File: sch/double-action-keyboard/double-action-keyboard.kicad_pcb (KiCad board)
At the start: 2 copper layers, 125 x 68 mm, 125 parts, among them U1 Pico

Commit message: ダイオードの配置と配線を行いました。
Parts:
- removed H1, H2, H3, H4: MountingHole_Pad, MountingHole:MountingHole_3.2mm_M3_Pad
- added C1: 1u, Capacitor_SMD:C_0603_1608Metric_Pad1.08x0.95mm_HandSolder, B.Cu at (96.5, 58.0)
- added C2: 1u, Capacitor_SMD:C_0603_1608Metric_Pad1.08x0.95mm_HandSolder, B.Cu at (98.1, 60.5)
- added C3: 1u, Capacitor_SMD:C_0603_1608Metric_Pad1.08x0.95mm_HandSolder, B.Cu at (101.0, 58.5)
- added C4: 1u, Capacitor_SMD:C_0603_1608Metric_Pad1.08x0.95mm_HandSolder, B.Cu at (82.1, 71.0)
- added C5: 1u, Capacitor_SMD:C_0603_1608Metric_Pad1.08x0.95mm_HandSolder, B.Cu at (74.6, 67.5)
- added C6: 1u, Capacitor_SMD:C_0603_1608Metric_Pad1.08x0.95mm_HandSolder, B.Cu at (77.1, 70.5)
- added D81: D, Diode_SMD:D_SOD-123, F.Cu at (143.8, 72.5)
- added J1: Conn_01x02, Connector_JST:JST_XH_B2B-XH-A_1x02_P2.50mm_Vertical, F.Cu at (137.8, 72.5)
- added R1: 10k, Resistor_SMD:R_0603_1608Metric_Pad0.98x0.95mm_HandSolder, B.Cu at (86.5, 69.6)
- added R2: 10k, Resistor_SMD:R_0603_1608Metric_Pad0.98x0.95mm_HandSolder, B.Cu at (89.0, 69.6)
- added R3: 10k, Resistor_SMD:R_0603_1608Metric_Pad0.98x0.95mm_HandSolder, B.Cu at (91.5, 69.6)
- added R7: 1k, Resistor_SMD:R_0603_1608Metric_Pad0.98x0.95mm_HandSolder, B.Cu at (66.0, 67.0)
- added R8: 0, Resistor_SMD:R_0603_1608Metric_Pad0.98x0.95mm_HandSolder, B.Cu at (97.9, 66.5)
- added REF1: MountingHole_3.2mm_M3, MountingHole:MountingHole_3.2mm_M3, F.Cu at (53.5, 53.5)
- added REF1: MountingHole_3.2mm_M3, MountingHole:MountingHole_3.2mm_M3, F.Cu at (140.0, 53.5)
- added REF1: MountingHole_3.2mm_M3, MountingHole:MountingHole_3.2mm_M3, F.Cu at (196.5, 118.5)
- added REF2: MountingHole_3.2mm_M3, MountingHole:MountingHole_3.2mm_M3, F.Cu at (53.5, 118.5)
- added U2: AQM1602XA-RN-GBW, AQM1602:AQM1602XA-RN-GBW, F.Cu at (97.4, 55.0)
- added U3: AQM1602Y-NLW-FBW, AQM1602:AQM1602Y-NLW-FBW, F.Cu at (81.2, 75.0)
- D1, D10, D11, D12, D13, D14, D15, D16, D17, D18, D19, D2, D20, D21, D22, D23, D24, D25, D26, D27, D28, D29, D3, D30, D31, D32, D33, D34, D35, D36, D37, D38, D39, D4, D40, D41, D42, D43, D44, D45, D46, D47, D48, D49, D5, D50, D51, D52, D53, D54, D55, D56, D57, D58, D59, D6, D60, D61, D62, D63, D64, D65, D66, D67, D68, D69, D7, D70, D71, D72, D73, D74, D75, D76, D77, D78, D79, D8, D80, D9: moved to B.Cu
- U1: footprint MCU_RaspberryPi_and_Boards:RPi_Pico_SMD_TH -> my_pico_smd:pico_no_dbg_smd_th
- moved D79 87.4 mm to (175.5, 115.5), turned to -90 degrees
- moved D80 87.1 mm to (180.5, 115.5), turned to -90 degrees
- moved D77 86.3 mm to (162.5, 115.5), turned to -90 degrees
- moved D78 86.1 mm to (167.5, 115.5), turned to -90 degrees
- moved D75 85.4 mm to (149.5, 115.5), turned to -90 degrees
- moved D76 85.1 mm to (154.5, 115.5), turned to -90 degrees
- moved D73 84.6 mm to (136.5, 115.5), turned to -90 degrees
- moved D74 84.3 mm to (141.5, 115.5), turned to -90 degrees
- moved D71 83.5 mm to (123.5, 115.5), turned to -90 degrees
- moved D72 83.3 mm to (128.5, 115.5), turned to -90 degrees
- moved D69 82.9 mm to (110.5, 115.5), turned to -90 degrees
- moved D70 82.4 mm to (115.5, 115.5), turned to -90 degrees
- moved D67 82.2 mm to (97.5, 115.5), turned to -90 degrees
- moved D68 81.9 mm to (102.5, 115.5), turned to -90 degrees
- moved D65 81.4 mm to (84.5, 115.5), turned to -90 degrees
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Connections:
- D11 pad 2: /COL0 -> /COL10
- D12 pad 2: /COL1 -> /COL11
- D13 pad 2: /COL2 -> /COL12
- D14 pad 2: /COL3 -> /COL13
- D15 pad 2: /COL4 -> /COL14
- D16 pad 2: /COL5 -> /COL15
- D17 pad 2: /COL6 -> /COL16
- D18 pad 2: /COL7 -> /COL17
- D19 pad 2: /COL8 -> /COL18
- D20 pad 2: /COL9 -> /COL19
- D31 pad 2: /COL0 -> /COL10
- D32 pad 2: /COL1 -> /COL11
- D33 pad 2: /COL2 -> /COL12
- D34 pad 2: /COL3 -> /COL13
- D35 pad 2: /COL4 -> /COL14
- D36 pad 2: /COL5 -> /COL15
- D37 pad 2: /COL6 -> /COL16
- D38 pad 2: /COL7 -> /COL17
- D39 pad 2: /COL8 -> /COL18
- D40 pad 2: /COL9 -> /COL19
- D51 pad 2: /COL0 -> /COL10
- D52 pad 2: /COL1 -> /COL11
- D53 pad 2: /COL2 -> /COL12
- D54 pad 2: /COL3 -> /COL13
- D55 pad 2: /COL4 -> /COL14
- D56 pad 2: /COL5 -> /COL15
- D57 pad 2: /COL6 -> /COL16
- D58 pad 2: /COL7 -> /COL17
- D59 pad 2: /COL8 -> /COL18
- D60 pad 2: /COL9 -> /COL19
- D71 pad 2: /COL0 -> /COL10
- D72 pad 2: /COL1 -> /COL11
- D73 pad 2: /COL2 -> /COL12
- D74 pad 2: /COL3 -> /COL13
- D75 pad 2: /COL4 -> /COL14
- D76 pad 2: /COL5 -> /COL15
- D77 pad 2: /COL6 -> /COL16
- D78 pad 2: /COL7 -> /COL17
- D79 pad 2: /COL8 -> /COL18
- D80 pad 2: /COL9 -> /COL19
- SW10 pad 3: /ROW1 -> /ROW0
- SW11 pad 3: /ROW2 -> /ROW1
- SW12 pad 3: /ROW2 -> /ROW1
- SW13 pad 3: /ROW2 -> /ROW1
- SW14 pad 3: /ROW2 -> /ROW1
- SW15 pad 3: /ROW2 -> /ROW1
- SW16 pad 3: /ROW3 -> /ROW1
- SW17 pad 3: /ROW3 -> /ROW1
- SW18 pad 3: /ROW3 -> /ROW1
- SW19 pad 3: /ROW3 -> /ROW1
- SW20 pad 3: /ROW3 -> /ROW1
- SW21 pad 3: /ROW4 -> /ROW2
- SW22 pad 3: /ROW4 -> /ROW2
- SW23 pad 3: /ROW4 -> /ROW2
- SW24 pad 3: /ROW4 -> /ROW2
- SW25 pad 3: /ROW4 -> /ROW2
- SW26 pad 3: /ROW5 -> /ROW2
- SW27 pad 3: /ROW5 -> /ROW2
- SW28 pad 3: /ROW5 -> /ROW2
- SW29 pad 3: /ROW5 -> /ROW2
- SW30 pad 3: /ROW5 -> /ROW2
- SW31 pad 3: /ROW6 -> /ROW3
- SW32 pad 3: /ROW6 -> /ROW3
- SW33 pad 3: /ROW6 -> /ROW3
- SW34 pad 3: /ROW6 -> /ROW3
- SW35 pad 3: /ROW6 -> /ROW3
- SW36 pad 3: /ROW7 -> /ROW3
- SW37 pad 3: /ROW7 -> /ROW3
- SW38 pad 3: /ROW7 -> /ROW3
- SW39 pad 3: /ROW7 -> /ROW3
- SW40 pad 3: /ROW7 -> /ROW3
- SW6 pad 3: /ROW1 -> /ROW0
- SW7 pad 3: /ROW1 -> /ROW0
- SW8 pad 3: /ROW1 -> /ROW0
- SW9 pad 3: /ROW1 -> /ROW0
- U1 pad 1: /COL0 -> /ROW3
- U1 pad 10: /COL7 -> /COL6
- U1 pad 11: /COL8 -> /COL5
- U1 pad 12: /COL9 -> /COL4
- U1 pad 14: /ROW0 -> /COL3
- U1 pad 15: /ROW1 -> /COL2
- U1 pad 16: /ROW2 -> /COL1
- U1 pad 17: /ROW3 -> /COL0
- U1 pad 19: /ROW4 -> /LCD_I2C_SDA
- U1 pad 2: /COL1 -> /ROW2
- U1 pad 20: /ROW5 -> /LCD_I2C_SCL
- U1 pad 21: /ROW7 -> /COL10
- U1 pad 22: /ROW6 -> /COL11
- U1 pad 24: unconnected-(U1-GPIO18-Pad24) -> /COL12
- U1 pad 25: unconnected-(U1-GPIO19-Pad25) -> /COL13
- U1 pad 26: unconnected-(U1-GPIO20-Pad26) -> /COL14
- U1 pad 27: unconnected-(U1-GPIO21-Pad27) -> /COL15
- U1 pad 29: unconnected-(U1-GPIO22-Pad29) -> /COL16
- U1 pad 31: unconnected-(U1-GPIO26_ADC0-Pad31) -> /COL17
- U1 pad 32: unconnected-(U1-GPIO27_ADC1-Pad32) -> /COL18
- U1 pad 34: unconnected-(U1-GPIO28_ADC2-Pad34) -> /COL19
- U1 pad 36: unconnected-(U1-3V3-Pad36) -> +3.3V
- U1 pad 39: unconnected-(U1-VSYS-Pad39) -> Net-(D81-K)
- U1 pad 4: /COL2 -> /ROW1
- U1 pad 5: /COL3 -> /ROW0
- U1 pad 6: /COL4 -> /COL9
- U1 pad 7: /COL5 -> /COL8
- U1 pad 9: /COL6 -> /COL7
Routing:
- net /ROW3: track 0.00 -> 220.6 mm
- net /ROW2: track 0.00 -> 208.0 mm
- net /ROW1: track 0.00 -> 193.2 mm
- net /ROW0: track 0.00 -> 180.1 mm
- net /COL0: track 0.00 -> 166.6 mm
- net +3.3V: track 0.00 -> 163.9 mm, vias 0 -> 2
- net /COL1: track 0.00 -> 162.1 mm
- net /COL2: track 0.00 -> 156.4 mm
- net /COL3: track 0.00 -> 154.2 mm
- net /COL4: track 0.00 -> 151.2 mm
- net /COL5: track 0.00 -> 148.8 mm
- net /COL6: track 0.00 -> 143.0 mm
- net /COL7: track 0.00 -> 140.9 mm
- net /COL8: track 0.00 -> 137.6 mm
- net /COL9: track 0.00 -> 136.1 mm
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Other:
- board size 125 x 68 mm -> 150 x 72 mm

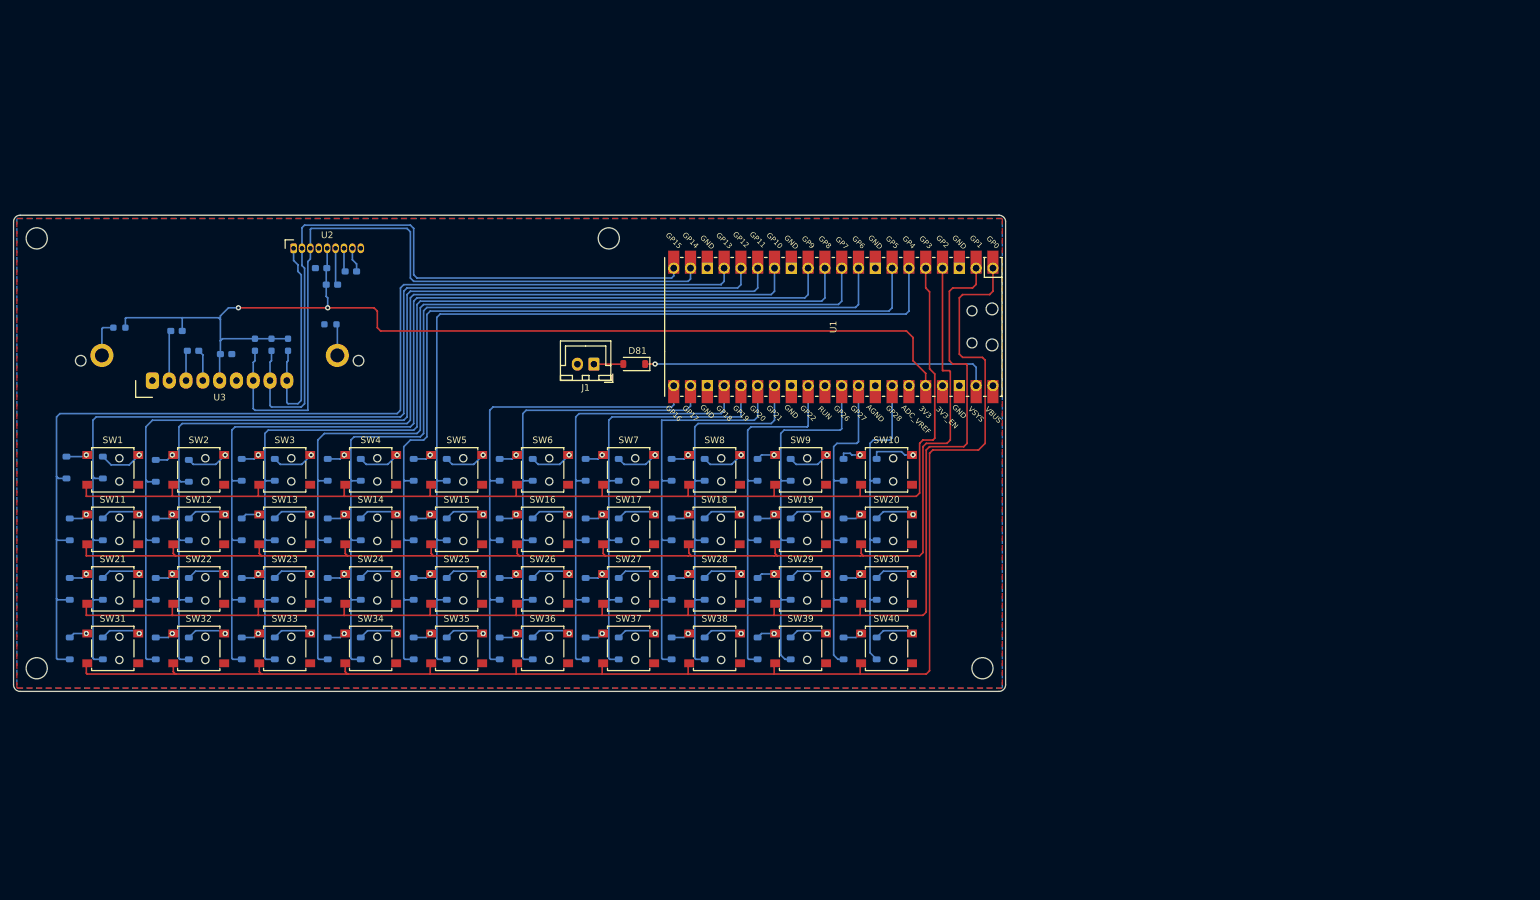
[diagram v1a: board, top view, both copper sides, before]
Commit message: KiCad 8.0にアップデートしました。 部品配置をやり直し中。
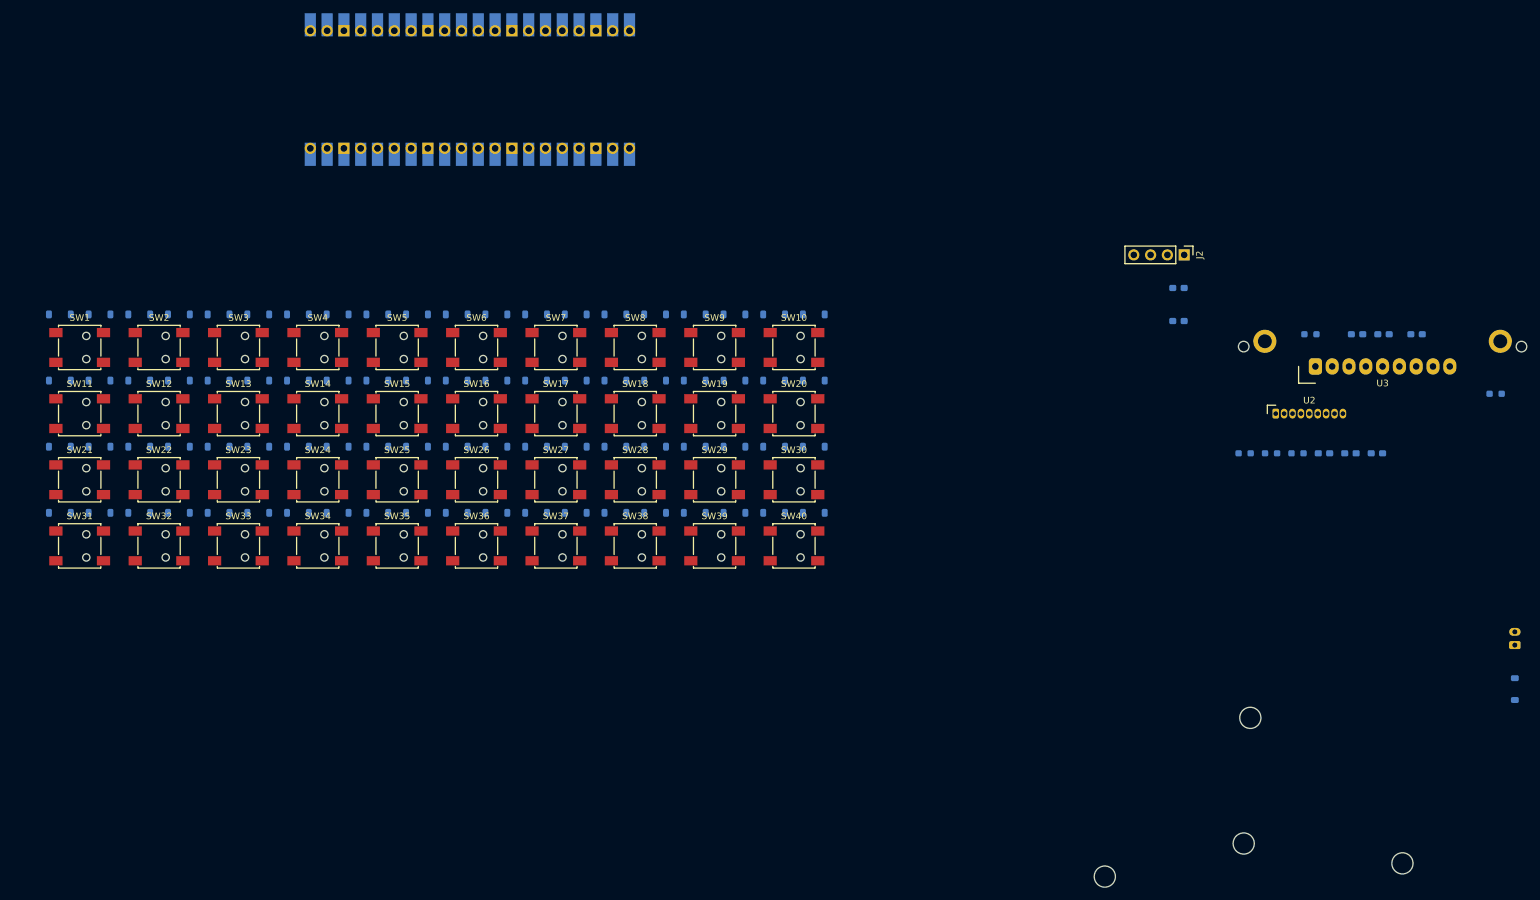
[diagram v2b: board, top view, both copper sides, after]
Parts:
- removed R7: 1k, Resistor_SMD:R_0603_1608Metric_Pad0.98x0.95mm_HandSolder
- removed R8: 0, Resistor_SMD:R_0603_1608Metric_Pad0.98x0.95mm_HandSolder
- added C7: 10u, Capacitor_SMD:C_0603_1608Metric_Pad1.08x0.95mm_HandSolder, B.Cu at (226.1, 61.0)
- added C8: 0.1u, Capacitor_SMD:C_0603_1608Metric_Pad1.08x0.95mm_HandSolder, B.Cu at (226.1, 66.0)
- added J2: Conn_01x04, Connector_PinHeader_2.54mm:PinHeader_1x04_P2.54mm_Vertical, F.Cu at (227.0, 56.0)
- added R4: 1k, Resistor_SMD:R_0603_1608Metric_Pad0.98x0.95mm_HandSolder, B.Cu at (246.1, 68.0)
- added R5: 0, Resistor_SMD:R_0603_1608Metric_Pad0.98x0.95mm_HandSolder, B.Cu at (274.1, 77.0)
- D1: value 1N4148W -> D
- D81: value D -> 1N4148W; moved to B.Cu
- J1: footprint Connector_JST:JST_XH_B2B-XH-A_1x02_P2.50mm_Vertical -> Connector_JST:JST_PH_B2B-PH-K_1x02_P2.00mm_Vertical; moved to B.Cu
- U1: moved to B.Cu
- moved D1 221.5 mm to (277.0, 121.7), turned to 90 degrees
- moved REF1 188.1 mm to (215.0, 150.0)
- moved REF2 184.4 mm to (236.0, 145.0)
- moved C4 180.0 mm to (262.1, 68.0)
- moved C6 180.0 mm to (257.1, 68.0)
- moved C5 178.5 mm to (253.1, 68.0)
- moved U3 175.9 mm to (257.0, 72.9)
- moved R1 158.5 mm to (244.1, 86.0), turned to 0 degrees
- moved C3 157.6 mm to (256.1, 86.0)
- moved C2 156.1 mm to (252.1, 86.0)
- moved C1 154.2 mm to (248.1, 86.0)
- moved REF1 152.7 mm to (260.0, 148.0)
- moved R2 152.0 mm to (240.1, 86.0), turned to 0 degrees
- moved U2 150.6 mm to (245.9, 80.0)
- moved J1 145.6 mm to (277.0, 115.0), turned to 90 degrees
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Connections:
- D1 pad 2: /COL0 -> Net-(D1-A)
- D10 pad 2: /COL9 -> /COL8
- D11 pad 2: /COL10 -> /COL9
- D12 pad 2: /COL11 -> /COL10
- D13 pad 2: /COL12 -> /COL11
- D14 pad 2: /COL13 -> /COL12
- D15 pad 2: /COL14 -> /COL13
- D16 pad 2: /COL15 -> /COL14
- D17 pad 2: /COL16 -> /COL15
- D18 pad 2: /COL17 -> /COL16
- D19 pad 2: /COL18 -> /COL17
- D2 pad 2: /COL1 -> /COL0
- D20 pad 2: /COL19 -> /COL18
- D21 pad 2: /COL0 -> /COL19
- D22 pad 2: /COL1 -> /COL0
- D23 pad 2: /COL2 -> /COL1
- D24 pad 2: /COL3 -> /COL2
- D25 pad 2: /COL4 -> /COL3
- D26 pad 2: /COL5 -> /COL4
- D27 pad 2: /COL6 -> /COL5
- D28 pad 2: /COL7 -> /COL6
- D29 pad 2: /COL8 -> /COL7
- D3 pad 2: /COL2 -> /COL1
- D30 pad 2: /COL9 -> /COL8
- D31 pad 2: /COL10 -> /COL9
- D32 pad 2: /COL11 -> /COL10
- D33 pad 2: /COL12 -> /COL11
- D34 pad 2: /COL13 -> /COL12
- D35 pad 2: /COL14 -> /COL13
- D36 pad 2: /COL15 -> /COL14
- D37 pad 2: /COL16 -> /COL15
- D38 pad 2: /COL17 -> /COL16
- D39 pad 2: /COL18 -> /COL17
- D4 pad 2: /COL3 -> /COL2
- D40 pad 2: /COL19 -> /COL18
- D41 pad 2: /COL0 -> /COL19
- D42 pad 2: /COL1 -> /COL0
- D43 pad 2: /COL2 -> /COL1
- D44 pad 2: /COL3 -> /COL2
- D45 pad 2: /COL4 -> /COL3
- D46 pad 2: /COL5 -> /COL4
- D47 pad 2: /COL6 -> /COL5
- D48 pad 2: /COL7 -> /COL6
- D49 pad 2: /COL8 -> /COL7
- D5 pad 2: /COL4 -> /COL3
- D50 pad 2: /COL9 -> /COL8
- D51 pad 2: /COL10 -> /COL9
- D52 pad 2: /COL11 -> /COL10
- D53 pad 2: /COL12 -> /COL11
- D54 pad 2: /COL13 -> /COL12
- D55 pad 2: /COL14 -> /COL13
- D56 pad 2: /COL15 -> /COL14
- D57 pad 2: /COL16 -> /COL15
- D58 pad 2: /COL17 -> /COL16
- D59 pad 2: /COL18 -> /COL17
- D6 pad 2: /COL5 -> /COL4
- D60 pad 2: /COL19 -> /COL18
- D61 pad 2: /COL0 -> /COL19
- D62 pad 2: /COL1 -> /COL0
- D63 pad 2: /COL2 -> /COL1
- D64 pad 2: /COL3 -> /COL2
- D65 pad 2: /COL4 -> /COL3
- D66 pad 2: /COL5 -> /COL4
- D67 pad 2: /COL6 -> /COL5
- D68 pad 2: /COL7 -> /COL6
- D69 pad 2: /COL8 -> /COL7
- D7 pad 2: /COL6 -> /COL5
- D70 pad 2: /COL9 -> /COL8
- D71 pad 2: /COL10 -> /COL9
- D72 pad 2: /COL11 -> /COL10
- D73 pad 2: /COL12 -> /COL11
- D74 pad 2: /COL13 -> /COL12
- D75 pad 2: /COL14 -> /COL13
- D76 pad 2: /COL15 -> /COL14
- D77 pad 2: /COL16 -> /COL15
- D78 pad 2: /COL17 -> /COL16
- D79 pad 2: /COL18 -> /COL17
- D8 pad 2: /COL7 -> /COL6
- D80 pad 2: /COL19 -> /COL18
- D81 pad 2: Net-(D81-A) -> /COL19
- D9 pad 2: /COL8 -> /COL7
- J1 pad 1: Net-(D81-A) -> Net-(D1-A)
- SW1 pad 1: Net-(D2-K) -> Net-(D3-K)
- SW1 pad 2: Net-(D1-K) -> Net-(D2-K)
- SW10 pad 1: Net-(D20-K) -> Net-(D21-K)
- SW10 pad 2: Net-(D19-K) -> Net-(D20-K)
- SW11 pad 1: Net-(D22-K) -> Net-(D23-K)
- SW11 pad 2: Net-(D21-K) -> Net-(D22-K)
- SW12 pad 1: Net-(D24-K) -> Net-(D25-K)
- SW12 pad 2: Net-(D23-K) -> Net-(D24-K)
- SW13 pad 1: Net-(D26-K) -> Net-(D27-K)
- SW13 pad 2: Net-(D25-K) -> Net-(D26-K)
- SW14 pad 1: Net-(D28-K) -> Net-(D29-K)
- SW14 pad 2: Net-(D27-K) -> Net-(D28-K)
- SW15 pad 1: Net-(D30-K) -> Net-(D31-K)
- SW15 pad 2: Net-(D29-K) -> Net-(D30-K)
- SW16 pad 1: Net-(D32-K) -> Net-(D33-K)
- SW16 pad 2: Net-(D31-K) -> Net-(D32-K)
- SW17 pad 1: Net-(D34-K) -> Net-(D35-K)
- SW17 pad 2: Net-(D33-K) -> Net-(D34-K)
- SW18 pad 1: Net-(D36-K) -> Net-(D37-K)
- SW18 pad 2: Net-(D35-K) -> Net-(D36-K)
- SW19 pad 1: Net-(D38-K) -> Net-(D39-K)
- SW19 pad 2: Net-(D37-K) -> Net-(D38-K)
- SW2 pad 1: Net-(D4-K) -> Net-(D5-K)
- SW2 pad 2: Net-(D3-K) -> Net-(D4-K)
- SW20 pad 1: Net-(D40-K) -> Net-(D41-K)
- SW20 pad 2: Net-(D39-K) -> Net-(D40-K)
- SW21 pad 1: Net-(D42-K) -> Net-(D43-K)
- SW21 pad 2: Net-(D41-K) -> Net-(D42-K)
- SW22 pad 1: Net-(D44-K) -> Net-(D45-K)
- SW22 pad 2: Net-(D43-K) -> Net-(D44-K)
- SW23 pad 1: Net-(D46-K) -> Net-(D47-K)
- SW23 pad 2: Net-(D45-K) -> Net-(D46-K)
- SW24 pad 1: Net-(D48-K) -> Net-(D49-K)
- SW24 pad 2: Net-(D47-K) -> Net-(D48-K)
- SW25 pad 1: Net-(D50-K) -> Net-(D51-K)
- SW25 pad 2: Net-(D49-K) -> Net-(D50-K)
- SW26 pad 1: Net-(D52-K) -> Net-(D53-K)
- SW26 pad 2: Net-(D51-K) -> Net-(D52-K)
- SW27 pad 1: Net-(D54-K) -> Net-(D55-K)
- SW27 pad 2: Net-(D53-K) -> Net-(D54-K)
- SW28 pad 1: Net-(D56-K) -> Net-(D57-K)
- SW28 pad 2: Net-(D55-K) -> Net-(D56-K)
- SW29 pad 1: Net-(D58-K) -> Net-(D59-K)
- SW29 pad 2: Net-(D57-K) -> Net-(D58-K)
- SW3 pad 1: Net-(D6-K) -> Net-(D7-K)
- SW3 pad 2: Net-(D5-K) -> Net-(D6-K)
- SW30 pad 1: Net-(D60-K) -> Net-(D61-K)
- SW30 pad 2: Net-(D59-K) -> Net-(D60-K)
- SW31 pad 1: Net-(D62-K) -> Net-(D63-K)
- SW31 pad 2: Net-(D61-K) -> Net-(D62-K)
- SW32 pad 1: Net-(D64-K) -> Net-(D65-K)
- SW32 pad 2: Net-(D63-K) -> Net-(D64-K)
- SW33 pad 1: Net-(D66-K) -> Net-(D67-K)
- SW33 pad 2: Net-(D65-K) -> Net-(D66-K)
- SW34 pad 1: Net-(D68-K) -> Net-(D69-K)
- SW34 pad 2: Net-(D67-K) -> Net-(D68-K)
- SW35 pad 1: Net-(D70-K) -> Net-(D71-K)
- SW35 pad 2: Net-(D69-K) -> Net-(D70-K)
- SW36 pad 1: Net-(D72-K) -> Net-(D73-K)
- SW36 pad 2: Net-(D71-K) -> Net-(D72-K)
- SW37 pad 1: Net-(D74-K) -> Net-(D75-K)
- SW37 pad 2: Net-(D73-K) -> Net-(D74-K)
- SW38 pad 1: Net-(D76-K) -> Net-(D77-K)
- SW38 pad 2: Net-(D75-K) -> Net-(D76-K)
- SW39 pad 1: Net-(D78-K) -> Net-(D79-K)
- SW39 pad 2: Net-(D77-K) -> Net-(D78-K)
- SW4 pad 1: Net-(D8-K) -> Net-(D9-K)
- SW4 pad 2: Net-(D7-K) -> Net-(D8-K)
- SW40 pad 1: Net-(D80-K) -> Net-(D81-K)
- SW40 pad 2: Net-(D79-K) -> Net-(D80-K)
- SW5 pad 1: Net-(D10-K) -> Net-(D11-K)
- SW5 pad 2: Net-(D9-K) -> Net-(D10-K)
- SW6 pad 1: Net-(D12-K) -> Net-(D13-K)
- SW6 pad 2: Net-(D11-K) -> Net-(D12-K)
- SW7 pad 1: Net-(D14-K) -> Net-(D15-K)
- SW7 pad 2: Net-(D13-K) -> Net-(D14-K)
- SW8 pad 1: Net-(D16-K) -> Net-(D17-K)
- SW8 pad 2: Net-(D15-K) -> Net-(D16-K)
- SW9 pad 1: Net-(D18-K) -> Net-(D19-K)
- SW9 pad 2: Net-(D17-K) -> Net-(D18-K)
- U1 pad 1: /ROW3 -> /LCD_I2C_SDA
- U1 pad 10: /COL6 -> /COL11
- U1 pad 11: /COL5 -> /COL12
- U1 pad 12: /COL4 -> /COL13
- U1 pad 14: /COL3 -> /COL14
- U1 pad 15: /COL2 -> /COL15
- U1 pad 16: /COL1 -> /COL16
- U1 pad 17: /COL0 -> /COL17
- U1 pad 19: /LCD_I2C_SDA -> /COL18
- U1 pad 2: /ROW2 -> /LCD_I2C_SCL
- U1 pad 20: /LCD_I2C_SCL -> /COL19
- U1 pad 21: /COL10 -> /COL5
- U1 pad 22: /COL11 -> /COL4
- U1 pad 24: /COL12 -> /COL3
- U1 pad 25: /COL13 -> /COL2
- U1 pad 26: /COL14 -> /COL1
- U1 pad 27: /COL15 -> /COL0
- U1 pad 29: /COL16 -> /ROW0
- U1 pad 31: /COL17 -> /ROW1
- U1 pad 32: /COL18 -> /ROW2
- U1 pad 34: /COL19 -> /ROW3
- U1 pad 39: Net-(D81-K) -> Net-(D1-K)
- U1 pad 4: /ROW1 -> /COL6
- U1 pad 5: /ROW0 -> /COL7
- U1 pad 6: /COL9 -> /COL8
- U1 pad 7: /COL8 -> /COL9
- U1 pad 9: /COL7 -> /COL10
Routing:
- net /ROW3: track 220.6 -> 0.00 mm
- net /ROW2: track 208.0 -> 0.00 mm
- net /ROW1: track 193.2 -> 0.00 mm
- net /ROW0: track 180.1 -> 0.00 mm
- net /COL0: track 166.6 -> 0.00 mm
- net +3.3V: track 163.9 -> 0.28 mm, vias 2 -> 0
- net /COL1: track 162.1 -> 0.00 mm
- net /COL2: track 156.4 -> 0.00 mm
- net /COL3: track 154.2 -> 0.00 mm
- net /COL4: track 151.2 -> 0.00 mm
- net /COL5: track 148.8 -> 0.00 mm
- net /COL6: track 143.0 -> 0.00 mm
- net /COL7: track 140.9 -> 0.00 mm
- net /COL8: track 137.6 -> 0.00 mm
- net /COL9: track 136.1 -> 0.00 mm
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- removed copper zone on B.Cu, net GND
- removed copper zone on F.Cu, net GND
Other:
- board outline removed

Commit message: ざっくり配線しました。 線間はもっと詰める予定。
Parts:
- added C10: 0.1u, Capacitor_SMD:C_0603_1608Metric_Pad1.08x0.95mm_HandSolder, B.Cu at (243.0, 60.0)
- added C9: 10u, Capacitor_SMD:C_0603_1608Metric_Pad1.08x0.95mm_HandSolder, B.Cu at (243.0, 64.0)
- added J3: Conn_01x04, Connector_PinHeader_2.54mm:PinHeader_1x04_P2.54mm_Vertical, F.Cu at (250.0, 56.0)
- added R6: 10k, Resistor_SMD:R_0603_1608Metric_Pad0.98x0.95mm_HandSolder, B.Cu at (156.0, 46.0)
- moved R1 151.8 mm to (106.0, 23.0)
- moved C1 148.7 mm to (110.0, 31.0)
- moved C2 148.7 mm to (114.0, 31.0)
- moved C3 148.7 mm to (118.0, 31.0)
- moved R3 148.4 mm to (100.0, 27.0)
- moved R2 147.4 mm to (106.0, 25.0)
- moved U2 141.8 mm to (114.0, 28.0)
- moved R5 116.6 mm to (162.0, 45.0)
- moved C4 114.3 mm to (150.0, 46.0)
- moved C5 113.3 mm to (142.0, 46.0)
- moved C6 113.3 mm to (146.0, 46.0)
- moved R4 111.7 mm to (137.0, 44.0)
- moved U3 109.6 mm to (150.0, 49.0)
- moved U1 40.8 mm to (80.0, 43.1)
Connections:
- U1 pad 29: /ROW0 -> /ROW3
- U1 pad 31: /ROW1 -> /ROW2
- U1 pad 32: /ROW2 -> /ROW1
- U1 pad 34: /ROW3 -> /ROW0
- U3 pad 9: Net-(U2-RES_N) -> Net-(U3-RES_N)
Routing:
- net /ROW3: track 0.00 -> 237.0 mm
- net /ROW2: track 0.00 -> 225.4 mm
- net /ROW1: track 0.00 -> 209.2 mm
- net /ROW0: track 0.00 -> 190.2 mm
- net /COL19: track 0.00 -> 128.8 mm
- net /COL17: track 0.00 -> 124.6 mm
- net /COL16: track 0.00 -> 120.9 mm
- net /COL15: track 0.00 -> 117.7 mm
- net /COL18: track 0.00 -> 115.6 mm
- net /COL14: track 0.00 -> 113.9 mm
- net /COL6: track 0.00 -> 113.6 mm
- net /COL13: track 0.00 -> 113.5 mm
- net /COL12: track 0.00 -> 109.7 mm
- net /COL7: track 0.00 -> 106.8 mm
- net /COL11: track 0.00 -> 106.0 mm
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- added copper zone on B.Cu, net GND
- added copper zone on F.Cu, net GND
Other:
- board outline added: 134 x 90 mm
